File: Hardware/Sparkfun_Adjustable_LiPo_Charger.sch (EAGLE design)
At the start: 27 parts, among them SW1 DIP-06, U1 MCP73831

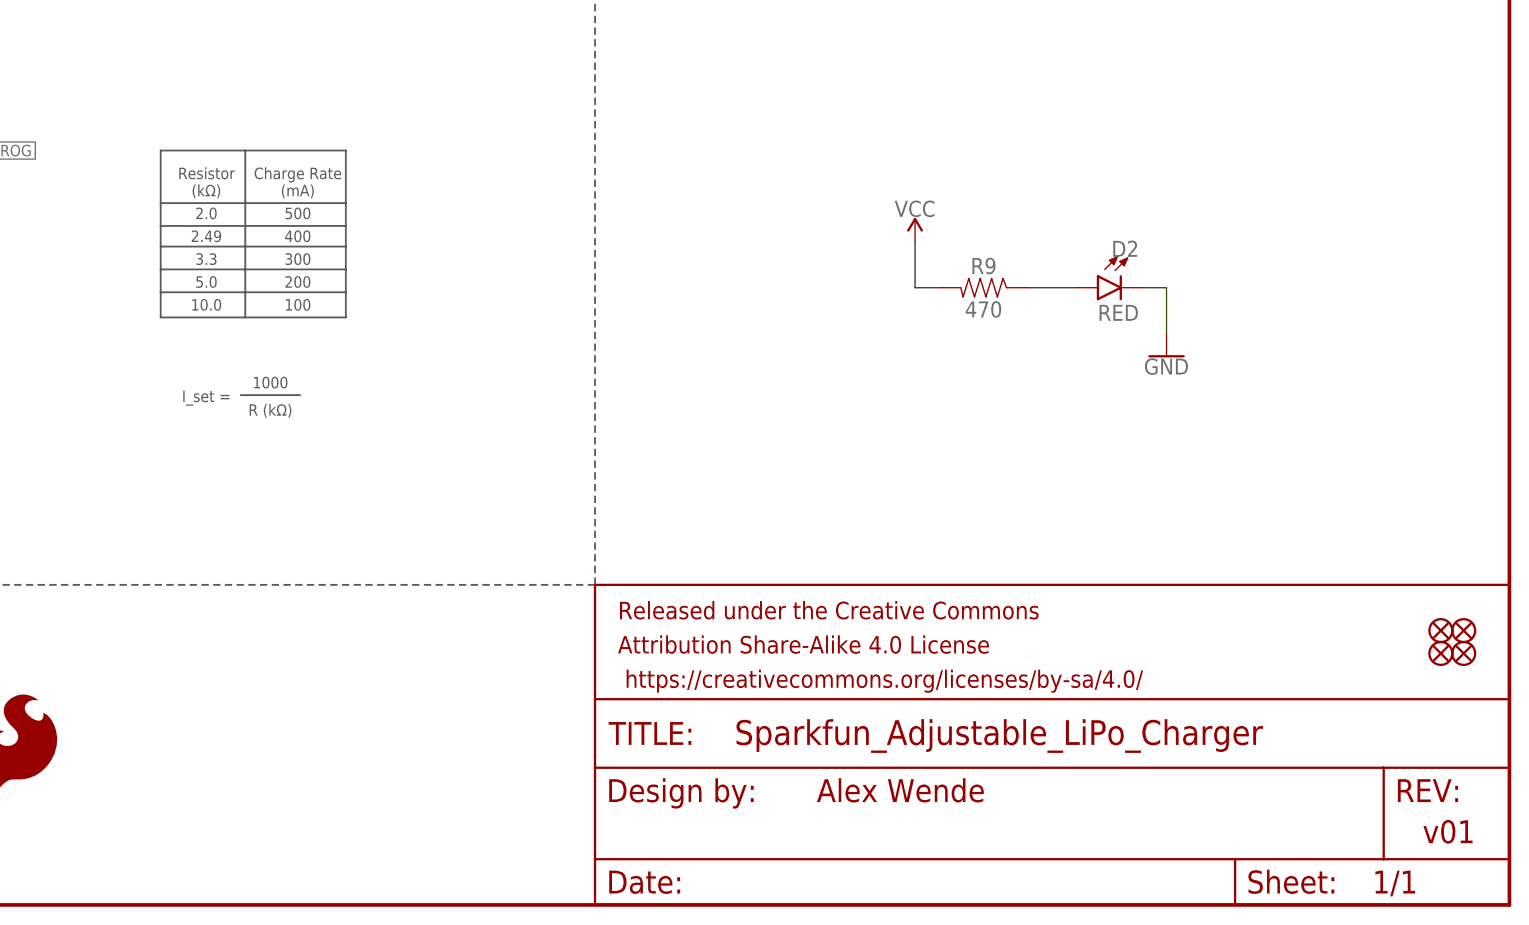
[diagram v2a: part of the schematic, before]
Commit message: v10 changes
- Added switch label to indicate on/off position.
- Added units to charge rate equation
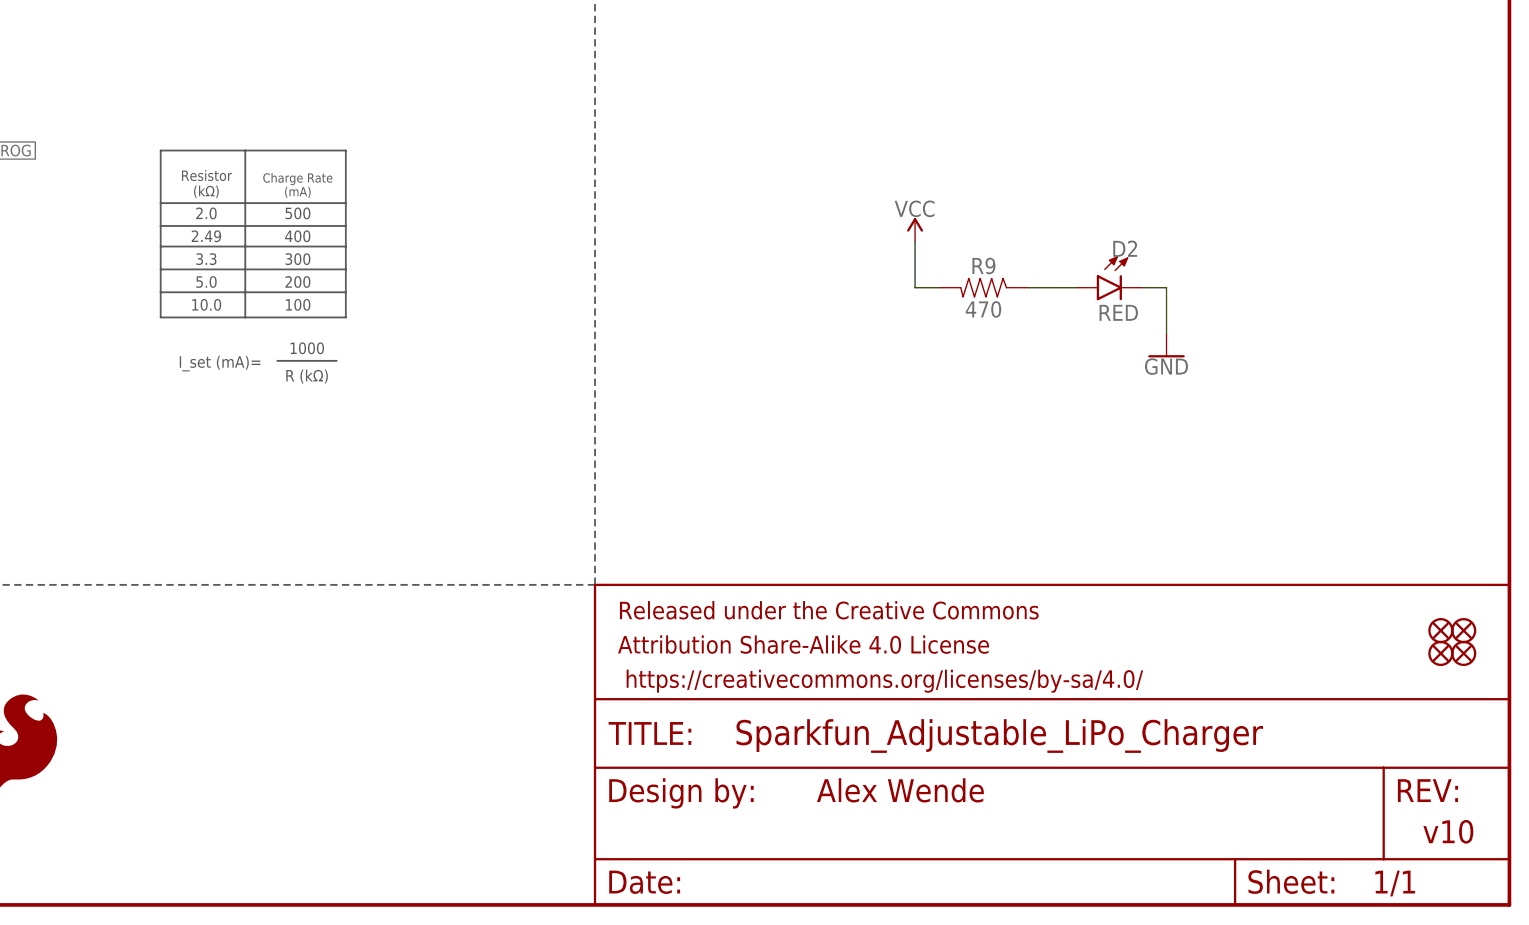
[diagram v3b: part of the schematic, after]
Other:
- note added: "I_set (mA)="
- note added: "v10"
- note removed: "I_set ="
- note removed: "v01"
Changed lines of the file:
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@@
 <wire x1="147.32" y1="35.56" x2="0" y2="35.56" width="0.2032" layer="97" style="shortdash"/>
 <text x="171.958" y="11.43" size="2.54" layer="94">Alex Wende</text>
-<text x="239.268" y="6.858" size="2.54" layer="94">v01</text>
+<text x="239.268" y="6.858" size="2.54" layer="94">v10</text>
 <text x="2.54" y="180.34" size="2.54" layer="97">Connectors</text>
 <text x="2.54" y="104.14" size="2.54" layer="97">Charge Rate Select</text>
-<text x="104.14" y="78.74" size="1.27" layer="97" align="bottom-center">Resistor
+<text x="104.14" y="78.74" size="1.143" layer="97" align="bottom-center">Resistor
 (kΩ)</text>
-<text x="114.3" y="78.74" size="1.27" layer="97" align="bottom-center">Charge Rate
+<text x="114.3" y="78.74" size="1.016" layer="97" align="bottom-center">Charge Rate
 (mA)</text>
 <text x="104.14" y="76.2" size="1.27" layer="97" align="bottom-center">2.0</text>
@@
 <wire x1="99.06" y1="68.072" x2="119.634" y2="68.072" width="0.2032" layer="97"/>
 <wire x1="108.458" y1="83.82" x2="108.458" y2="65.278" width="0.2032" layer="97"/>
-<text x="104.14" y="55.88" size="1.27" layer="97" align="bottom-center">I_set =</text>
-<text x="111.252" y="57.404" size="1.27" layer="97" align="bottom-center">1000</text>
-<text x="111.252" y="54.356" size="1.27" layer="97" align="bottom-center">R (kΩ)</text>
-<wire x1="107.95" y1="56.642" x2="114.554" y2="56.642" width="0.2032" layer="97"/>
+<text x="105.664" y="59.69" size="1.27" layer="97" align="bottom-center">I_set (mA)= </text>
+<text x="115.316" y="61.214" size="1.27" layer="97" align="bottom-center">1000</text>
+<text x="115.316" y="58.166" size="1.27" layer="97" align="bottom-center">R (kΩ)</text>
+<wire x1="112.014" y1="60.452" x2="118.618" y2="60.452" width="0.2032" layer="97"/>
 <text x="149.86" y="180.34" size="2.54" layer="97">LiPo Charger</text>
 <wire x1="147.32" y1="109.22" x2="248.92" y2="109.22" width="0.2032" layer="97" style="shortdash"/>
